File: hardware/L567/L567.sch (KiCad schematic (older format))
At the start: 2 parts, among them J1 1st HALF, J2 2nd HALF

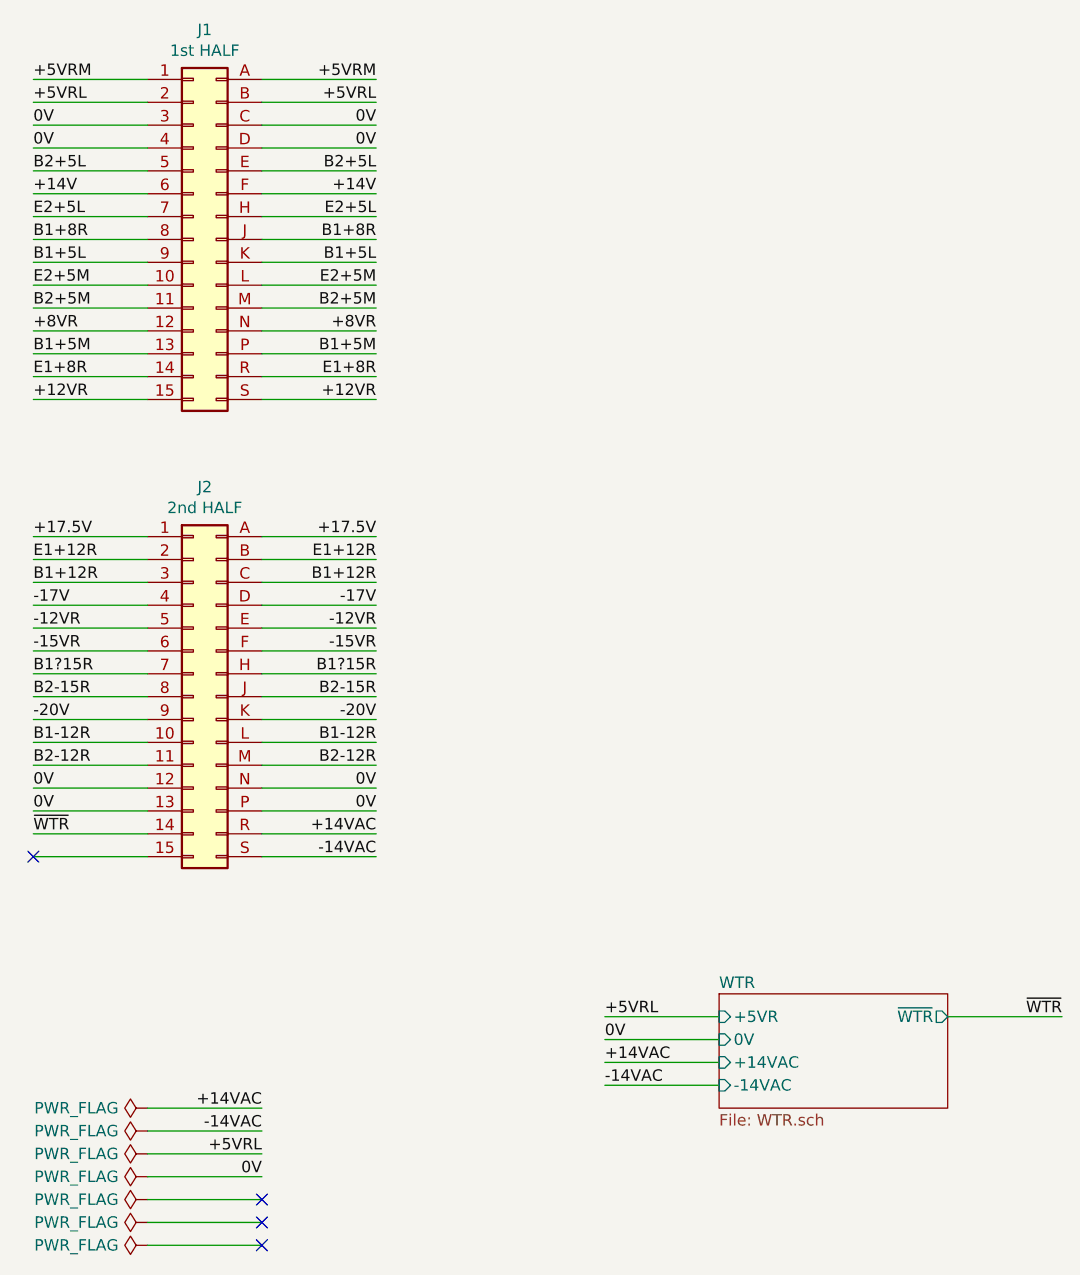
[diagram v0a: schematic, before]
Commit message: some power supply updates
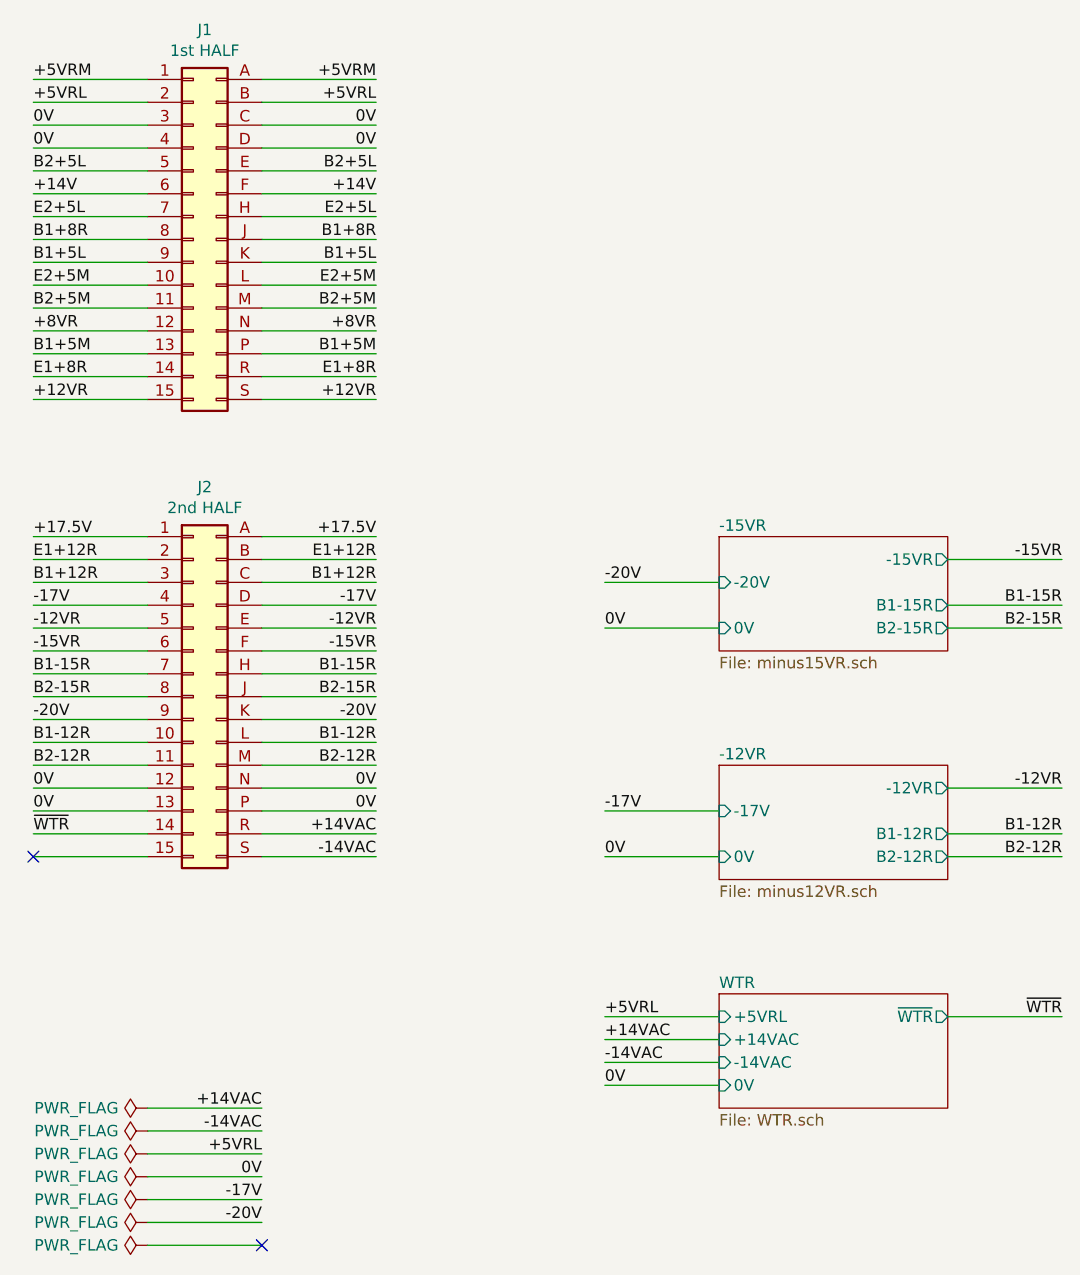
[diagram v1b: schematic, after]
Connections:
- net B1?15R renamed B1-15R
- no-connect marks 4 -> 2
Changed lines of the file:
@@
 $Descr A4 11693 8268
 encoding utf-8
-Sheet 1 2
+Sheet 1 4
 Title ""
 Date ""
@@
 -15VR
 Text Label 2500 3600 2    50   ~ 0
-B1?15R
+B1-15R
 Text Label 2500 3700 2    50   ~ 0
 B2-15R
@@
 -15VR
 Text Label 1000 3600 0    50   ~ 0
-B1?15R
+B1-15R
 Text Label 1000 3700 0    50   ~ 0
 B2-15R
@@
 F0 "WTR" 50
 F1 "WTR.sch" 50
-F2 "+5VR" I L 4000 5100 50
-F3 "0V" I L 4000 5200 50
+F2 "+5VRL" I L 4000 5100 50
+F3 "0V" I L 4000 5400 50
 F4 "~WTR" O R 5000 5100 50
-F5 "-14VAC" I L 4000 5400 50
-F6 "+14VAC" I L 4000 5300 50
+F5 "-14VAC" I L 4000 5300 50
+F6 "+14VAC" I L 4000 5200 50
 $EndSheet
 Wire Wire Line
 	3500 5100 4000 5100
 Wire Wire Line
+	3500 5400 4000 5400
+Wire Wire Line
 	3500 5200 4000 5200
 Wire Wire Line
 	3500 5300 4000 5300
-Wire Wire Line
-	3500 5400 4000 5400
 Wire Wire Line
 	5000 5100 5500 5100
@@
 +5VRL
 Text Label 3500 5200 0    50   ~ 0
-0V
++14VAC
 Text Label 3500 5300 0    50   ~ 0
-+14VAC
-Text Label 3500 5400 0    50   ~ 0
 -14VAC
 Text Label 5500 5100 2    50   ~ 0
@@
 Text Label 2000 5600 2    50   ~ 0
 -14VAC
-NoConn ~ 2000 5900
-NoConn ~ 2000 6000
 NoConn ~ 2000 6100
 Text Label 2000 5700 2    50   ~ 0
@@
 Text Label 2000 5800 2    50   ~ 0
 0V
+$Sheet
+S 4000 4000 1000 500
+U 60554B2F
+F0 "-12VR" 50
+F1 "minus12VR.sch" 50
+F2 "-17V" I L 4000 4200 50
+F3 "0V" I L 4000 4400 50
+F4 "B1-12R" O R 5000 4300 50
+F5 "B2-12R" O R 5000 4400 50
+F6 "-12VR" O R 5000 4100 50
+$EndSheet
+Text Label 3500 5400 0    50   ~ 0
+0V
+Wire Wire Line
+	3500 4200 4000 4200
+Wire Wire Line
+	3500 4400 4000 4400
+Text Label 3500 4200 0    50   ~ 0
+-17V
+Text Label 3500 4400 0    50   ~ 0
+0V
+Wire Wire Line
+	5500 4100 5000 4100
+Wire Wire Line
+	5500 4300 5000 4300
+Wire Wire Line
+	5500 4400 5000 4400
+Text Label 5500 4100 2    50   ~ 0
+-12VR
+Text Label 5500 4300 2    50   ~ 0
+B1-12R
+Text Label 5500 4400 2    50   ~ 0
+B2-12R
+Wire Wire Line
+	3500 3200 4000 3200
+Wire Wire Line
+	3500 3400 4000 3400
+Text Label 3500 3200 0    50   ~ 0
+-20V
+Text Label 3500 3400 0    50   ~ 0
+0V
+Wire Wire Line
+	5500 3100 5000 3100
+Wire Wire Line
+	5500 3300 5000 3300
+Wire Wire Line
+	5500 3400 5000 3400
+Text Label 5500 3100 2    50   ~ 0
+-15VR
+Text Label 5500 3300 2    50   ~ 0
+B1-15R
+Text Label 5500 3400 2    50   ~ 0
+B2-15R
+$Sheet
+S 4000 3000 1000 500
+U 6059F5EE
+F0 "-15VR" 50
+F1 "minus15VR.sch" 50
+F2 "-20V" I L 4000 3200 50
+F3 "0V" I L 4000 3400 50
+F4 "B1-15R" O R 5000 3300 50
+F5 "B2-15R" O R 5000 3400 50
+F6 "-15VR" O R 5000 3100 50
+$EndSheet
+Text Label 2000 5900 2    50   ~ 0
+-17V
+Text Label 2000 6000 2    50   ~ 0
+-20V
 $EndSCHEMATC
